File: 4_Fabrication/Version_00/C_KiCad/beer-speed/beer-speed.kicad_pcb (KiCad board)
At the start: 2 copper layers, 11 parts, among them J1 Conn_02x03_Odd_Even, P1 LCD-S401C52TR, SW1 EG1213, SW2 TM1000Q, U1 ATmega4809-A, Y1 Crystal 8MHz

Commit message: first placement
first placement on KiaCad PCB
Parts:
- P1: moved to B.Cu
- moved SW1 65.3 mm to (104.1, 55.9), turned to 270 degrees
- moved U1 61.2 mm to (120.7, 59.7)
- moved SW2 58.3 mm to (110.5, 64.8)
- moved NT1 46.4 mm to (138.4, 57.1)
- moved R1 45.9 mm to (120.7, 48.3)
- moved P1 44.9 mm to (109.2, 39.4)
- moved J1 43.2 mm to (111.8, 49.5), turned to 180 degrees
- moved C2 35.5 mm to (137.2, 52.1), turned to 270 degrees
- moved Y1 35.3 mm to (132.1, 57.1), turned to 270 degrees
- moved C1 35.1 mm to (137.2, 62.2), turned to 270 degrees
- moved BT1 14.2 mm to (149.9, 64.8), turned to 90 degrees

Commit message: KiCad PCB V0
First version of KiCad PCB
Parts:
- added H1: MountingHole, MountingHole:MountingHole_3.2mm_M3, F.Cu at (92.7, 73.7)
- added H2: MountingHole, MountingHole:MountingHole_3.2mm_M3, F.Cu at (92.7, 110.5)
- added H3: MountingHole, MountingHole:MountingHole_3.2mm_M3, F.Cu at (148.6, 73.7)
- added H4: MountingHole, MountingHole:MountingHole_3.2mm_M3, F.Cu at (148.6, 110.5)
- moved C1 39.0 mm to (124.5, 99.1)
- moved C2 39.0 mm to (124.5, 88.9)
- moved NT1 39.0 mm to (125.7, 94.0)
- moved P1 39.0 mm to (96.5, 76.2)
- moved R1 39.0 mm to (108.0, 85.1)
- moved Y1 39.0 mm to (119.4, 94.0)
- moved BT1 39.0 mm to (137.2, 101.6)
- moved J1 39.0 mm to (99.1, 86.4)
- moved U1 39.0 mm to (108.0, 96.5)
- moved SW1 39.0 mm to (91.4, 92.7)
- moved SW2 39.0 mm to (97.8, 101.6)
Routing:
- net GND: track 0.00 -> 100.6 mm, vias 0 -> 46
- net Net-(BT1-Pad1): track 0.00 -> 85.0 mm
- net 4B: track 0.00 -> 71.8 mm
- net 4C: track 0.00 -> 68.0 mm
- net 4D: track 0.00 -> 64.6 mm
- net 4E: track 0.00 -> 61.1 mm
- net 3C: track 0.00 -> 58.7 mm, vias 0 -> 1
- net 3E: track 0.00 -> 54.0 mm, vias 0 -> 3
- net 3D: track 0.00 -> 53.3 mm, vias 0 -> 3
- net +3V0: track 0.00 -> 50.9 mm, vias 0 -> 2
- net 1B: track 0.00 -> 49.9 mm, vias 0 -> 4
- net 1A: track 0.00 -> 45.3 mm, vias 0 -> 4
- net 1G: track 0.00 -> 45.3 mm, vias 0 -> 1
- net 1F: track 0.00 -> 44.3 mm, vias 0 -> 1
- net 3B: track 0.00 -> 41.9 mm, vias 0 -> 1
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- added copper zone on B.Cu, net GND
- added copper zone on F.Cu, net GND
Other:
- board outline added: 63.5 x 44.5 mm

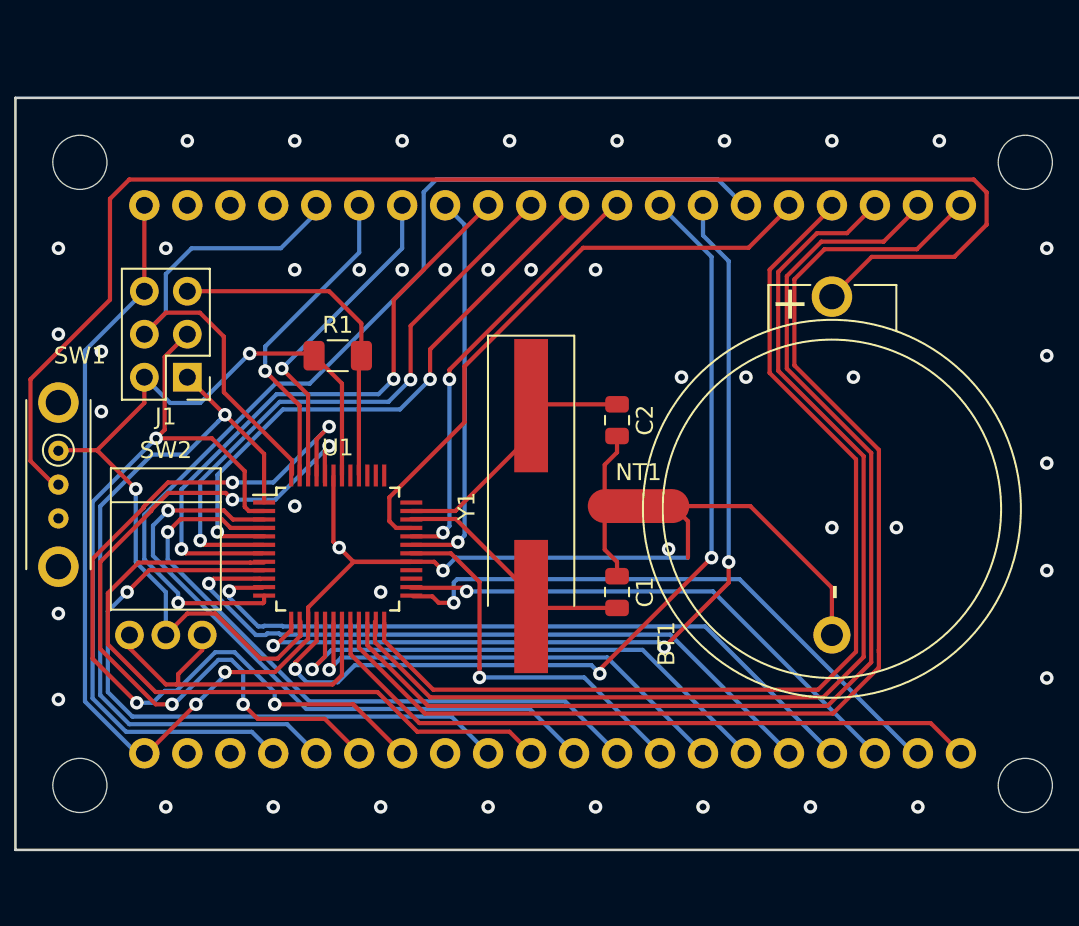
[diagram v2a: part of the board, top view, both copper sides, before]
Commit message: add text on PCB + img
add TITLE on PCB
add name on PCB
add 2 img of 3d PCB on 1_DOCUMENTATION
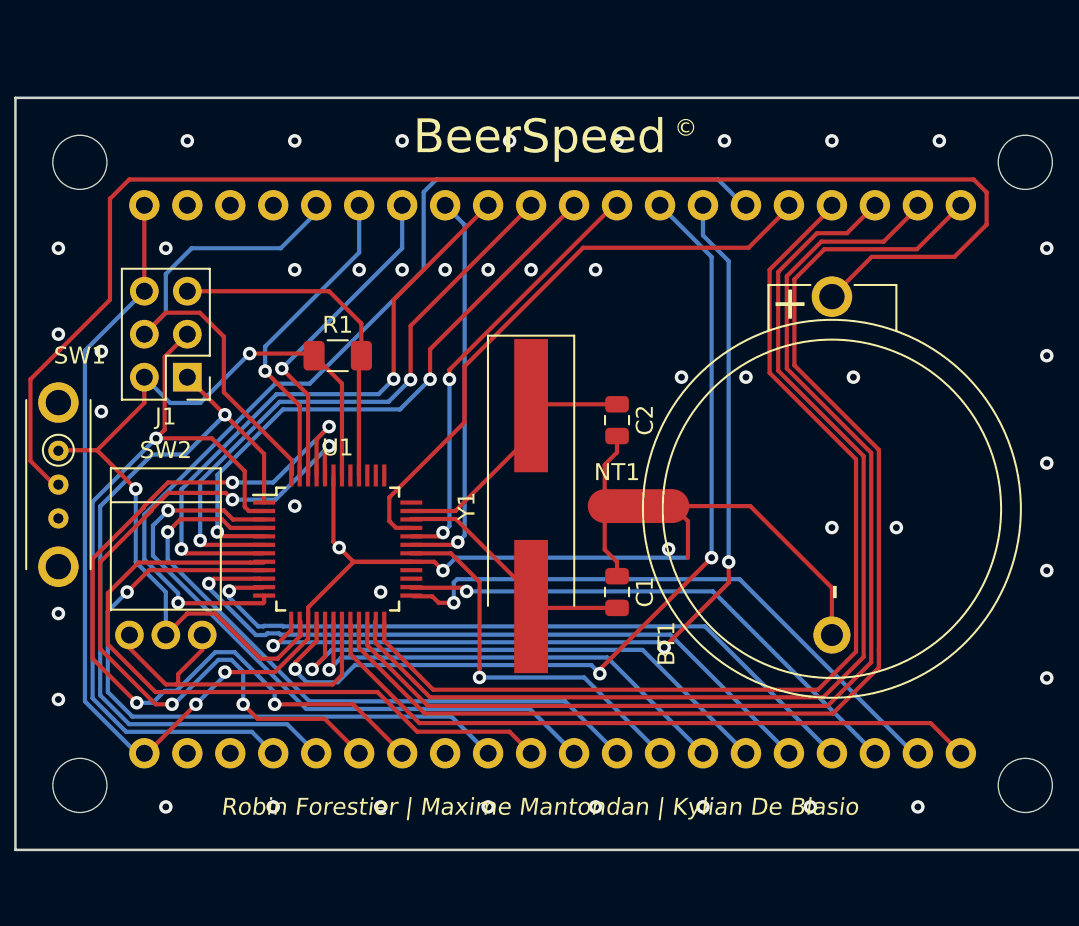
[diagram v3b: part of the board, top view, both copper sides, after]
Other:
- board text added: "BeerSpeed"
- board text added: "Robin Forestier | Maxime Mantondan | Kylian De Blasio"
- board text added: "©"

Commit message: PCB
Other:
- board text added: "Bottom"
- board text added: "N°__"
- board text added: "Top"
- board text added: "V0"
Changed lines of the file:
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@@
   (general
     (thickness 1.6)
-    (drawings 11)
+    (drawings 15)
     (tracks 472)
     (zones 0)
@@
     )
   )
+  (gr_text N°__ (at 102 73) (layer F.SilkS)
+    (effects (font (size 1.5 1.5) (thickness 0.3)))
+  )
+  (gr_text V0 (at 144 112) (layer F.SilkS)
+    (effects (font (size 1 1) (thickness 0.25)))
+  )
+  (gr_text Bottom (at 140 72) (layer B.SilkS)
+    (effects (font (size 1.5 1.5) (thickness 0.3)) (justify mirror))
+  )
+  (gr_text Top (at 140 72) (layer F.SilkS)
+    (effects (font (size 1.5 1.5) (thickness 0.3)))
+  )
   (gr_text © (at 128.524 71.628) (layer F.SilkS)
